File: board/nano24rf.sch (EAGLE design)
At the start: 16 parts

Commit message: wsitch!
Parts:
- added JP6: (no value), ATTAMI-V0.00:HEADER-1X2ROUND
- added SW1: (no value), microbuilder:SWITCH_SPST
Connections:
- removed net VOUT: D1.C, D2.C, FET1.1, FET2.1
- new net VIN: D1.C, D2.C, FET1.1, FET2.1, JP1.15, SW1.S
- net GND: now also JP6.2; no longer JP1.13
- net RAW: now also JP6.1, SW1.P; no longer JP1.15
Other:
- note added: "D13 3v3 GND A0 A1 A2 A3 A4 A5 A6 A7 5V RESET GND VIN"
- note removed: "D13 3v3 GND A0 A1 A2 A3 A4 A5 A6 A7 5V GND GND RAW"
- moved on the sheet: JP5
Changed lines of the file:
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@@
 <part name="JP4" library="adafruit" deviceset="PINHD-2X4" device=""/>
 <part name="JP5" library="adafruit" deviceset="PINHD-2X4" device=""/>
+<part name="SW1" library="microbuilder" deviceset="SWITCH_SPST" device=""/>
+<part name="JP6" library="ATTAMI-V0.00" deviceset="HEADER-1X2" device="ROUND"/>
 </parts>
 <sheets>
@@
 A7
 5V
+RESET
 GND
-GND
-RAW</text>
+VIN</text>
 <text x="-2.54" y="-38.1" size="1.778" layer="91">https://github.com/shenkarSElab/nano24rf
 nice nano pintout -&gt; http://christianto.tjahyadi.com/wp-content/uploads/2014/11/nano.jpg</text>
@@
 <instance part="R4" gate="G$1" x="27.94" y="55.88" rot="R90"/>
 <instance part="JP4" gate="A" x="2.54" y="48.26"/>
-<instance part="JP5" gate="A" x="2.54" y="83.82"/>
+<instance part="JP5" gate="A" x="2.54" y="33.02"/>
+<instance part="SW1" gate="G$1" x="139.7" y="-5.08" smashed="yes">
+<attribute name="NAME" x="130.175" y="-8.89" size="1.27" layer="95"/>
+<attribute name="VALUE" x="134.62" y="-1.27" size="1.27" layer="96"/>
+</instance>
+<instance part="JP6" gate="G$1" x="152.4" y="15.24"/>
 </instances>
 <busses>
@@
 </segment>
 <segment>
-<pinref part="JP1" gate="G$1" pin="13"/>
-<wire x1="43.18" y1="35.56" x2="33.02" y2="35.56" width="0.1524" layer="91"/>
-</segment>
-<segment>
 <pinref part="JP1" gate="G$1" pin="3"/>
 <wire x1="43.18" y1="60.96" x2="33.02" y2="60.96" width="0.1524" layer="91"/>
+</segment>
+<segment>
+<pinref part="JP6" gate="G$1" pin="2"/>
+<wire x1="137.16" y1="15.24" x2="149.86" y2="15.24" width="0.1524" layer="91"/>
+<label x="137.16" y="15.24" size="1.778" layer="95"/>
 </segment>
 </net>
@@
 <net name="RAW" class="0">
 <segment>
-<pinref part="JP1" gate="G$1" pin="15"/>
-<wire x1="43.18" y1="30.48" x2="33.02" y2="30.48" width="0.1524" layer="91"/>
-<label x="33.02" y="27.94" size="1.778" layer="95"/>
+<wire x1="134.62" y1="-5.08" x2="127" y2="-5.08" width="0.1524" layer="91"/>
+<label x="127" y="-5.08" size="1.778" layer="95"/>
+<pinref part="SW1" gate="G$1" pin="P"/>
+</segment>
+<segment>
+<pinref part="JP6" gate="G$1" pin="1"/>
+<wire x1="149.86" y1="17.78" x2="137.16" y2="17.78" width="0.1524" layer="91"/>
+<label x="137.16" y="17.78" size="1.778" layer="95"/>
 </segment>
 </net>
@@
 <wire x1="68.58" y1="50.8" x2="76.2" y2="50.8" width="0.1524" layer="91"/>
 <label x="73.66" y="50.8" size="1.778" layer="95"/>
-</segment>
-</net>
-<net name="VOUT" class="0">
-<segment>
-<pinref part="D2" gate="D" pin="C"/>
-<wire x1="91.44" y1="10.16" x2="91.44" y2="2.54" width="0.1524" layer="91"/>
-<pinref part="FET2" gate="G$1" pin="1"/>
-<wire x1="91.44" y1="2.54" x2="104.14" y2="2.54" width="0.1524" layer="91"/>
-<junction x="91.44" y="2.54"/>
-<label x="91.44" y="10.16" size="1.778" layer="95"/>
-</segment>
-<segment>
-<pinref part="D1" gate="D" pin="C"/>
-<pinref part="FET1" gate="G$1" pin="1"/>
-<wire x1="50.8" y1="2.54" x2="38.1" y2="2.54" width="0.1524" layer="91"/>
-<wire x1="38.1" y1="2.54" x2="38.1" y2="10.16" width="0.1524" layer="91"/>
-<junction x="38.1" y="2.54"/>
-<label x="38.1" y="10.16" size="1.778" layer="95"/>
 </segment>
 </net>
@@
 </segment>
 </net>
+<net name="VIN" class="0">
+<segment>
+<pinref part="D2" gate="D" pin="C"/>
+<wire x1="91.44" y1="10.16" x2="91.44" y2="2.54" width="0.1524" layer="91"/>
+<pinref part="FET2" gate="G$1" pin="1"/>
+<wire x1="91.44" y1="2.54" x2="104.14" y2="2.54" width="0.1524" layer="91"/>
+<junction x="91.44" y="2.54"/>
+<label x="91.44" y="10.16" size="1.778" layer="95"/>
+</segment>
+<segment>
+<pinref part="D1" gate="D" pin="C"/>
+<pinref part="FET1" gate="G$1" pin="1"/>
+<wire x1="50.8" y1="2.54" x2="38.1" y2="2.54" width="0.1524" layer="91"/>
+<wire x1="38.1" y1="2.54" x2="38.1" y2="10.16" width="0.1524" layer="91"/>
+<junction x="38.1" y="2.54"/>
+<label x="38.1" y="10.16" size="1.778" layer="95"/>
+</segment>
+<segment>
+<pinref part="JP1" gate="G$1" pin="15"/>
+<wire x1="43.18" y1="30.48" x2="33.02" y2="30.48" width="0.1524" layer="91"/>
+<label x="33.02" y="27.94" size="1.778" layer="95"/>
+</segment>
+<segment>
+<pinref part="SW1" gate="G$1" pin="S"/>
+<wire x1="142.24" y1="-5.08" x2="149.86" y2="-5.08" width="0.1524" layer="91"/>
+<label x="144.78" y="-5.08" size="1.778" layer="95"/>
+</segment>
+</net>

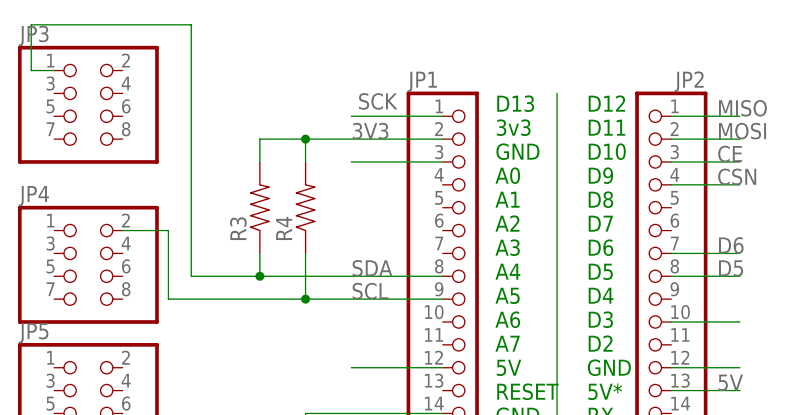
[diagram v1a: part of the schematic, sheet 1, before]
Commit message: slikscreens
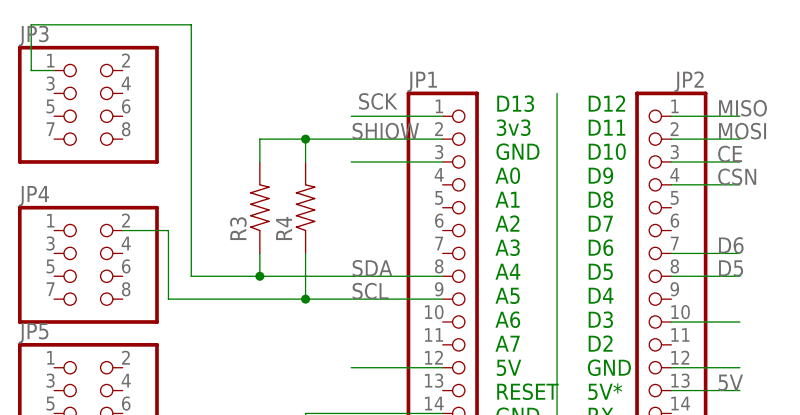
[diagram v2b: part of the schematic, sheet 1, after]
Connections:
- net 3V3 renamed SHIOW
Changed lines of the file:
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@@
 <grid distance="0.1" unitdist="inch" unit="mil" style="lines" multiple="1" display="no" altdistance="50" altunitdist="mil" altunit="mil"/>
 <layers>
-<layer number="1" name="Top" color="4" fill="1" visible="no" active="no"/>
-<layer number="2" name="Route2" color="1" fill="3" visible="no" active="no"/>
-<layer number="3" name="Route3" color="4" fill="3" visible="no" active="no"/>
-<layer number="4" name="Route4" color="1" fill="4" visible="no" active="no"/>
-<layer number="5" name="Route5" color="4" fill="4" visible="no" active="no"/>
-<layer number="6" name="Route6" color="1" fill="8" visible="no" active="no"/>
-<layer number="7" name="Route7" color="4" fill="8" visible="no" active="no"/>
-<layer number="8" name="Route8" color="1" fill="2" visible="no" active="no"/>
-<layer number="9" name="Route9" color="4" fill="2" visible="no" active="no"/>
-<layer number="10" name="Route10" color="1" fill="7" visible="no" active="no"/>
-<layer number="11" name="Route11" color="4" fill="7" visible="no" active="no"/>
-<layer number="12" name="Route12" color="1" fill="5" visible="no" active="no"/>
-<layer number="13" name="Route13" color="4" fill="5" visible="no" active="no"/>
-<layer number="14" name="Route14" color="1" fill="6" visible="no" active="no"/>
-<layer number="15" name="Route15" color="4" fill="6" visible="no" active="no"/>
-<layer number="16" name="Bottom" color="1" fill="1" visible="no" active="no"/>
-<layer number="17" name="Pads" color="2" fill="1" visible="no" active="no"/>
-<layer number="18" name="Vias" color="2" fill="1" visible="no" active="no"/>
-<layer number="19" name="Unrouted" color="6" fill="1" visible="no" active="no"/>
-<layer number="20" name="Dimension" color="15" fill="1" visible="no" active="no"/>
-<layer number="21" name="tPlace" color="7" fill="1" visible="no" active="no"/>
-<layer number="22" name="bPlace" color="7" fill="1" visible="no" active="no"/>
-<layer number="23" name="tOrigins" color="15" fill="1" visible="no" active="no"/>
-<layer number="24" name="bOrigins" color="15" fill="1" visible="no" active="no"/>
-<layer number="25" name="tNames" color="7" fill="1" visible="no" active="no"/>
-<layer number="26" name="bNames" color="7" fill="1" visible="no" active="no"/>
-<layer number="27" name="tValues" color="7" fill="1" visible="no" active="no"/>
-<layer number="28" name="bValues" color="7" fill="1" visible="no" active="no"/>
+<layer number="1" name="Top" color="4" fill="1" visible="yes" active="no"/>
+<layer number="2" name="Route2" color="1" fill="3" visible="yes" active="no"/>
+<layer number="3" name="Route3" color="4" fill="3" visible="yes" active="no"/>
+<layer number="4" name="Route4" color="1" fill="4" visible="yes" active="no"/>
+<layer number="5" name="Route5" color="4" fill="4" visible="yes" active="no"/>
+<layer number="6" name="Route6" color="1" fill="8" visible="yes" active="no"/>
+<layer number="7" name="Route7" color="4" fill="8" visible="yes" active="no"/>
+<layer number="8" name="Route8" color="1" fill="2" visible="yes" active="no"/>
+<layer number="9" name="Route9" color="4" fill="2" visible="yes" active="no"/>
+<layer number="10" name="Route10" color="1" fill="7" visible="yes" active="no"/>
+<layer number="11" name="Route11" color="4" fill="7" visible="yes" active="no"/>
+<layer number="12" name="Route12" color="1" fill="5" visible="yes" active="no"/>
+<layer number="13" name="Route13" color="4" fill="5" visible="yes" active="no"/>
+<layer number="14" name="Route14" color="1" fill="6" visible="yes" active="no"/>
+<layer number="15" name="Route15" color="4" fill="6" visible="yes" active="no"/>
+<layer number="16" name="Bottom" color="1" fill="1" visible="yes" active="no"/>
+<layer number="17" name="Pads" color="2" fill="1" visible="yes" active="no"/>
+<layer number="18" name="Vias" color="2" fill="1" visible="yes" active="no"/>
+<layer number="19" name="Unrouted" color="6" fill="1" visible="yes" active="no"/>
+<layer number="20" name="Dimension" color="15" fill="1" visible="yes" active="no"/>
+<layer number="21" name="tPlace" color="7" fill="1" visible="yes" active="no"/>
+<layer number="22" name="bPlace" color="7" fill="1" visible="yes" active="no"/>
+<layer number="23" name="tOrigins" color="15" fill="1" visible="yes" active="no"/>
+<layer number="24" name="bOrigins" color="15" fill="1" visible="yes" active="no"/>
+<layer number="25" name="tNames" color="7" fill="1" visible="yes" active="no"/>
+<layer number="26" name="bNames" color="7" fill="1" visible="yes" active="no"/>
+<layer number="27" name="tValues" color="7" fill="1" visible="yes" active="no"/>
+<layer number="28" name="bValues" color="7" fill="1" visible="yes" active="no"/>
 <layer number="29" name="tStop" color="7" fill="3" visible="no" active="no"/>
 <layer number="30" name="bStop" color="7" fill="6" visible="no" active="no"/>
@@
 <layer number="35" name="tGlue" color="7" fill="4" visible="no" active="no"/>
 <layer number="36" name="bGlue" color="7" fill="5" visible="no" active="no"/>
-<layer number="37" name="tTest" color="7" fill="1" visible="no" active="no"/>
-<layer number="38" name="bTest" color="7" fill="1" visible="no" active="no"/>
+<layer number="37" name="tTest" color="7" fill="1" visible="yes" active="no"/>
+<layer number="38" name="bTest" color="7" fill="1" visible="yes" active="no"/>
 <layer number="39" name="tKeepout" color="4" fill="11" visible="no" active="no"/>
 <layer number="40" name="bKeepout" color="1" fill="11" visible="no" active="no"/>
@@
 <layer number="44" name="Drills" color="7" fill="1" visible="no" active="no"/>
 <layer number="45" name="Holes" color="7" fill="1" visible="no" active="no"/>
-<layer number="46" name="Milling" color="3" fill="1" visible="no" active="no"/>
-<layer number="47" name="Measures" color="7" fill="1" visible="no" active="no"/>
-<layer number="48" name="Document" color="7" fill="1" visible="no" active="no"/>
-<layer number="49" name="Reference" color="7" fill="1" visible="no" active="no"/>
-<layer number="50" name="dxf" color="7" fill="1" visible="no" active="no"/>
-<layer number="51" name="tDocu" color="7" fill="1" visible="no" active="no"/>
-<layer number="52" name="bDocu" color="7" fill="1" visible="no" active="no"/>
-<layer number="53" name="tGND_GNDA" color="7" fill="9" visible="no" active="no"/>
-<layer number="54" name="bGND_GNDA" color="1" fill="9" visible="no" active="no"/>
-<layer number="56" name="wert" color="7" fill="1" visible="no" active="no"/>
-<layer number="57" name="tCAD" color="7" fill="1" visible="no" active="no"/>
+<layer number="46" name="Milling" color="3" fill="1" visible="yes" active="no"/>
+<layer number="47" name="Measures" color="7" fill="1" visible="yes" active="no"/>
+<layer number="48" name="Document" color="7" fill="1" visible="yes" active="no"/>
+<layer number="49" name="Reference" color="7" fill="1" visible="yes" active="no"/>
+<layer number="50" name="dxf" color="7" fill="1" visible="yes" active="no"/>
+<layer number="51" name="tDocu" color="7" fill="1" visible="yes" active="no"/>
+<layer number="52" name="bDocu" color="7" fill="1" visible="yes" active="no"/>
+<layer number="53" name="tGND_GNDA" color="7" fill="9" visible="yes" active="no"/>
+<layer number="54" name="bGND_GNDA" color="1" fill="9" visible="yes" active="no"/>
+<layer number="56" name="wert" color="7" fill="1" visible="yes" active="no"/>
+<layer number="57" name="tCAD" color="7" fill="1" visible="yes" active="no"/>
 <layer number="90" name="Modules" color="5" fill="1" visible="yes" active="yes"/>
 <layer number="91" name="Nets" color="2" fill="1" visible="yes" active="yes"/>
@@
 </segment>
 </net>
-<net name="3V3" class="0">
+<net name="SHIOW" class="0">
 <segment>
 <pinref part="JP1" gate="G$1" pin="2"/>

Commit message: before reomval of swith for fnr24
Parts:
- removed JP4, JP5: (no value), adafruit:PINHD-2X4
- added C1, C2: (no value), ATTAMI-V0.00:CAP0805
- added CN1, CN2, CN3, I2CPORT: 1X4-CLEANBIG, adafruit:1X4-CLEANBIG
- added SJ1, SJ2: JUMPER-PAD-3-2OF3_NC_BY_TRACE_SMALL, ATTAMI-V0.00:JUMPER-PAD-3-2OF3_NC_BY_TRACE_SMALL
- added SW2: (no value), microbuilder:SWITCH_SPST
- added U2: (no value), microbuilder:VREG_SOT23SOT23_WIDE
- JP3: device adafruit:PINHD-2X4 -> adafruit:PINHD-1X1CB
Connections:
- removed net SHIOW: JP1.2, R3.2, R4.2, U$2.VCC
- new net 3V3: JP1.2, R3.2, R4.2, SJ1.3, SJ2.1
- new net N$6: SJ1.2, SW2.S
- new net N$9: I2CPORT.4, SJ2.2
- new net RST: JP2.13
- new net V-ADJ: C2.1, SJ1.1, U2.VOUT
- new net V-NRF: SW2.P, U$2.VCC
- net 5V: now also C1.1, SJ2.3, U2.VIN; no longer JP2.13
- net D3: now also R1.1; no longer R2.1
- net D5: now also R2.1; no longer R1.1
- net GND: now also C1.2, C2.2, I2CPORT.1, U2.GND
- net RAW: now also JP3.1
- net SCL: now also I2CPORT.2; no longer JP4.2
- net SDA: now also I2CPORT.3; no longer JP3.1
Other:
- note added: "D12 D11 D10 D9 D8 D7 D6 D5 D4 D3 D2 GND rst RX TX"
- note removed: "D12 D11 D10 D9 D8 D7 D6 D5 D4 D3 D2 GND 5V* RX TX"

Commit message: more output
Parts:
- removed SW2: (no value), microbuilder:SWITCH_SPST
- added CN4: 1X4-CLEANBIG, adafruit:1X4-CLEANBIG
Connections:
- removed net N$9: I2CPORT.4, SJ2.2
- new net RX: CN4.3, JP2.14
- new net TX: CN4.2, JP2.15
- net 5V: now also CN4.1
- net GND: now also CN4.4, I2CPORT.4; no longer I2CPORT.1
- net N$6: now also I2CPORT.3, SJ2.2; no longer SJ1.2, SW2.S
- net SCL: now also I2CPORT.1; no longer I2CPORT.2
- net SDA: now also I2CPORT.2; no longer I2CPORT.3
- net V-NRF: now also SJ1.2; no longer SW2.P
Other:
- moved on the sheet: SJ2
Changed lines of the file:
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@@
 <part name="C1" library="ATTAMI-V0.00" deviceset="CAP" device="0805"/>
 <part name="C2" library="ATTAMI-V0.00" deviceset="CAP" device="0805"/>
-<part name="SW2" library="microbuilder" deviceset="SWITCH_SPST" device=""/>
 <part name="I2CPORT" library="adafruit" deviceset="1X4" device="-CLEANBIG"/>
 <part name="CN2" library="adafruit" deviceset="1X4" device="-CLEANBIG"/>
@@
 <part name="JP3" library="adafruit" deviceset="PINHD-1X1" device="CB"/>
 <part name="SJ2" library="ATTAMI-V0.00" deviceset="JUMPER-PAD-3-2OF3_NC_BY_TRACE" device="_SMALL" value=""/>
+<part name="CN4" library="adafruit" deviceset="1X4" device="-CLEANBIG"/>
 </parts>
 <sheets>
@@
 <attribute name="VALUE" x="159.004" y="56.261" size="1.778" layer="96"/>
 </instance>
-<instance part="SW2" gate="G$1" x="99.06" y="63.5" smashed="yes" rot="R90">
-<attribute name="NAME" x="95.885" y="62.23" size="1.27" layer="95" rot="R180"/>
-<attribute name="VALUE" x="95.25" y="58.42" size="1.27" layer="96" rot="R90"/>
-</instance>
 <instance part="I2CPORT" gate="G$1" x="-27.94" y="45.72" smashed="yes" rot="R180">
 <attribute name="NAME" x="-33.02" y="38.1" size="1.27" layer="95" font="vector"/>
@@
 </instance>
 <instance part="JP3" gate="G$1" x="152.4" y="5.08"/>
-<instance part="SJ2" gate="G$1" x="-12.7" y="50.8" smashed="yes">
-<attribute name="NAME" x="-9.779" y="54.61" size="1.778" layer="95" rot="R270"/>
+<instance part="SJ2" gate="G$1" x="-12.7" y="48.26" smashed="yes">
+<attribute name="NAME" x="-9.779" y="52.07" size="1.778" layer="95" rot="R270"/>
+</instance>
+<instance part="CN4" gate="G$1" x="10.16" y="10.16" smashed="yes" rot="R180">
+<attribute name="NAME" x="5.08" y="2.54" size="1.27" layer="95" font="vector"/>
 </instance>
 </instances>
@@
 </segment>
 <segment>
-<pinref part="I2CPORT" gate="G$1" pin="1"/>
-<wire x1="-17.78" y1="43.18" x2="-22.86" y2="43.18" width="0.1524" layer="91"/>
-<label x="-22.86" y="43.18" size="1.778" layer="95"/>
+<pinref part="CN4" gate="G$1" pin="4"/>
+<wire x1="15.24" y1="15.24" x2="20.32" y2="15.24" width="0.1524" layer="91"/>
+<label x="17.78" y="15.24" size="1.778" layer="95"/>
+</segment>
+<segment>
+<pinref part="I2CPORT" gate="G$1" pin="4"/>
+<wire x1="-22.86" y1="50.8" x2="-17.78" y2="50.8" width="0.1524" layer="91"/>
+<label x="-22.86" y="50.8" size="1.778" layer="95"/>
 </segment>
 </net>
@@
 <segment>
 <pinref part="SJ2" gate="G$1" pin="1"/>
-<wire x1="-12.7" y1="55.88" x2="-12.7" y2="60.96" width="0.1524" layer="91"/>
-<label x="-12.7" y="58.42" size="1.778" layer="95"/>
+<wire x1="-12.7" y1="53.34" x2="-12.7" y2="60.96" width="0.1524" layer="91"/>
+<label x="-12.7" y="55.88" size="1.778" layer="95"/>
 </segment>
 </net>
@@
 <segment>
 <pinref part="SJ2" gate="G$1" pin="3"/>
-<wire x1="-12.7" y1="45.72" x2="-12.7" y2="40.64" width="0.1524" layer="91"/>
-<label x="-12.7" y="43.18" size="1.778" layer="95"/>
+<wire x1="-12.7" y1="43.18" x2="-12.7" y2="38.1" width="0.1524" layer="91"/>
+<label x="-12.7" y="40.64" size="1.778" layer="95"/>
+</segment>
+<segment>
+<pinref part="CN4" gate="G$1" pin="1"/>
+<wire x1="15.24" y1="7.62" x2="20.32" y2="7.62" width="0.1524" layer="91"/>
+<label x="17.78" y="7.62" size="1.778" layer="95"/>
 </segment>
 </net>
@@
 </segment>
 <segment>
-<label x="-22.86" y="48.26" size="1.778" layer="95"/>
-<pinref part="I2CPORT" gate="G$1" pin="3"/>
-<wire x1="-17.78" y1="48.26" x2="-22.86" y2="48.26" width="0.1524" layer="91"/>
+<label x="-22.86" y="45.72" size="1.778" layer="95"/>
+<pinref part="I2CPORT" gate="G$1" pin="2"/>
+<wire x1="-17.78" y1="45.72" x2="-22.86" y2="45.72" width="0.1524" layer="91"/>
 </segment>
 </net>
@@
 </segment>
 <segment>
-<label x="-22.86" y="45.72" size="1.778" layer="95"/>
-<pinref part="I2CPORT" gate="G$1" pin="2"/>
-<wire x1="-17.78" y1="45.72" x2="-22.86" y2="45.72" width="0.1524" layer="91"/>
+<label x="-22.86" y="43.18" size="1.778" layer="95"/>
+<pinref part="I2CPORT" gate="G$1" pin="1"/>
+<wire x1="-22.86" y1="43.18" x2="-17.78" y2="43.18" width="0.1524" layer="91"/>
 </segment>
 </net>
@@
 <pinref part="U$2" gate="G$1" pin="VCC"/>
 <label x="99.06" y="53.34" size="1.778" layer="95"/>
-<pinref part="SW2" gate="G$1" pin="P"/>
-<wire x1="99.06" y1="58.42" x2="99.06" y2="46.99" width="0.1524" layer="91"/>
+<wire x1="99.06" y1="66.04" x2="99.06" y2="46.99" width="0.1524" layer="91"/>
+<pinref part="SJ1" gate="G$1" pin="2"/>
 </segment>
 </net>
@@
 </segment>
 </net>
-<net name="N$6" class="0">
-<segment>
-<pinref part="SJ1" gate="G$1" pin="2"/>
-<pinref part="SW2" gate="G$1" pin="S"/>
-</segment>
-</net>
 <net name="RST" class="0">
 <segment>
@@
 </segment>
 </net>
-<net name="N$9" class="0">
-<segment>
-<pinref part="I2CPORT" gate="G$1" pin="4"/>
+<net name="RX" class="0">
+<segment>
+<pinref part="CN4" gate="G$1" pin="3"/>
+<wire x1="15.24" y1="12.7" x2="20.32" y2="12.7" width="0.1524" layer="91"/>
+<label x="17.78" y="12.7" size="1.778" layer="95"/>
+</segment>
+<segment>
+<pinref part="JP2" gate="G$1" pin="14"/>
+<wire x1="68.58" y1="33.02" x2="76.2" y2="33.02" width="0.1524" layer="91"/>
+<label x="73.66" y="33.02" size="1.778" layer="95"/>
+</segment>
+</net>
+<net name="TX" class="0">
+<segment>
+<pinref part="CN4" gate="G$1" pin="2"/>
+<wire x1="15.24" y1="10.16" x2="20.32" y2="10.16" width="0.1524" layer="91"/>
+<label x="17.78" y="10.16" size="1.778" layer="95"/>
+</segment>
+<segment>
+<pinref part="JP2" gate="G$1" pin="15"/>
+<wire x1="68.58" y1="30.48" x2="76.2" y2="30.48" width="0.1524" layer="91"/>
+<label x="73.66" y="30.48" size="1.778" layer="95"/>
+</segment>
+</net>
+<net name="N$6" class="0">
+<segment>
+<pinref part="I2CPORT" gate="G$1" pin="3"/>
 <pinref part="SJ2" gate="G$1" pin="2"/>
-<wire x1="-22.86" y1="50.8" x2="-17.78" y2="50.8" width="0.1524" layer="91"/>
-</segment>
-</net>
+<wire x1="-22.86" y1="48.26" x2="-17.78" y2="48.26" width="0.1524" layer="91"/>
+</segment>
+</net>
